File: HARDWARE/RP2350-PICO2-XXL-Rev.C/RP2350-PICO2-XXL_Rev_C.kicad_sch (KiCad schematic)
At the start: 83 parts, among them Q1 Q12MHz/18pF/30ppm/4P/3.2x2.5m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, U1 W25Q128JVSIQ(SOIC-8_208mils), U2 TPS62A02ADRLR(SOT-563-6), U3 RP2350B(QFN-80_10.00x10.00x0.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, U4 NA(W25Q128JVSIQ(SOIC-8_208mil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, U5 APS6404L-3SQR-SN(SOIC-8_150mi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

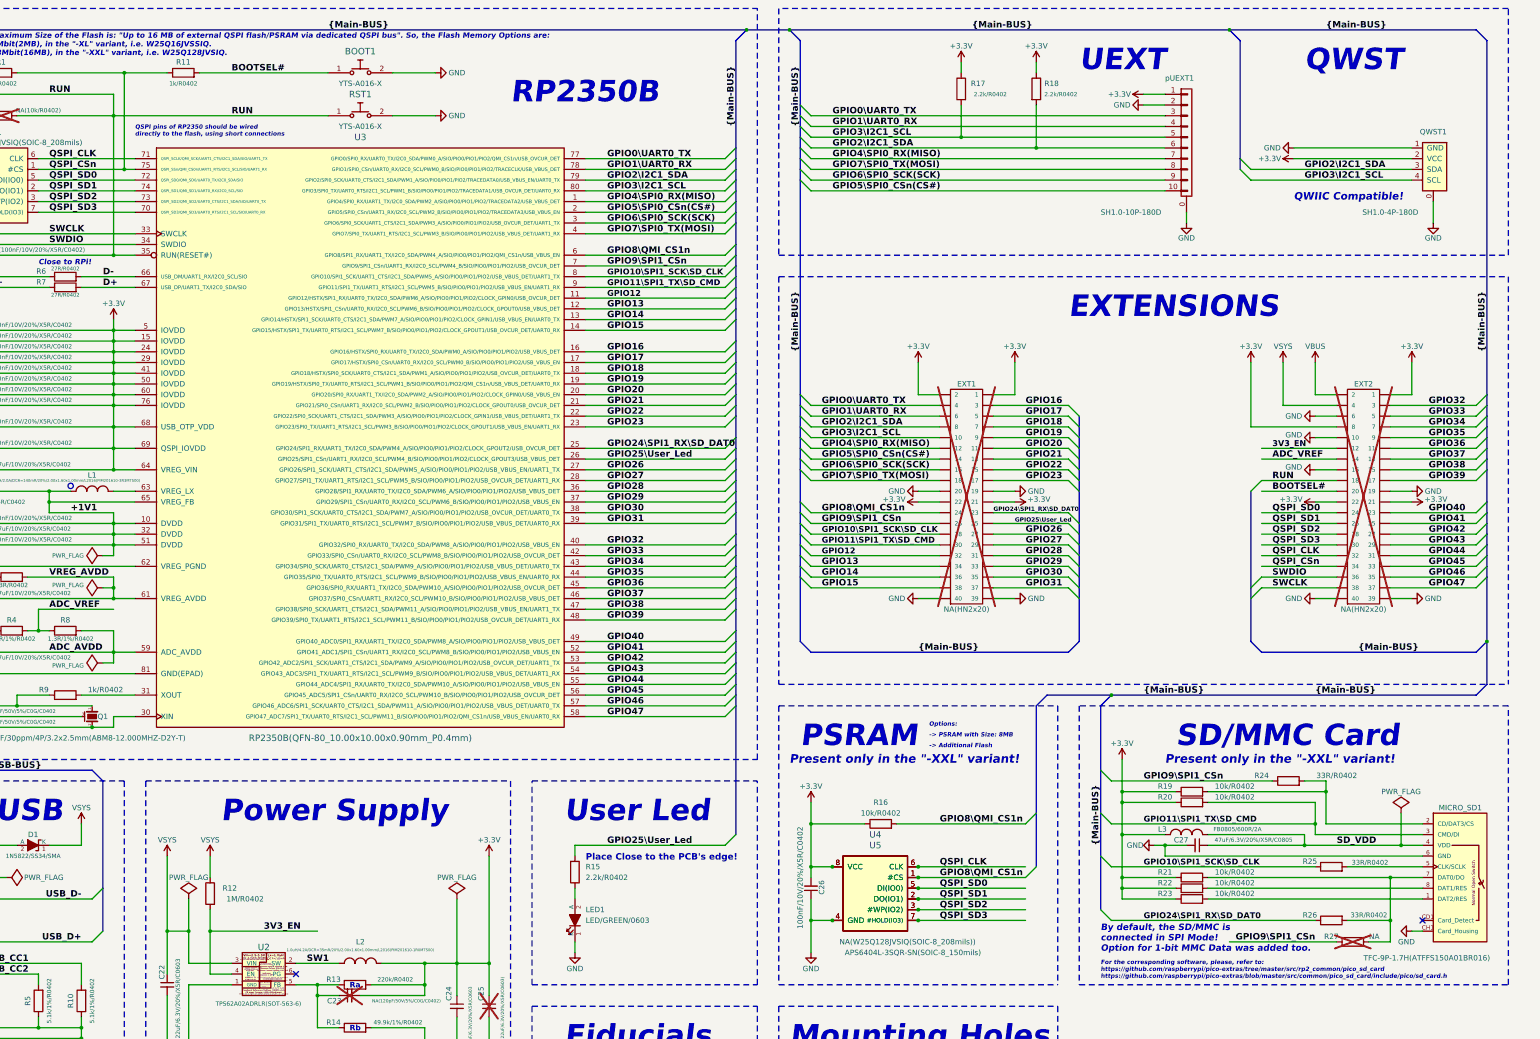
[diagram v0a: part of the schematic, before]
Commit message: removing unneeded connectors
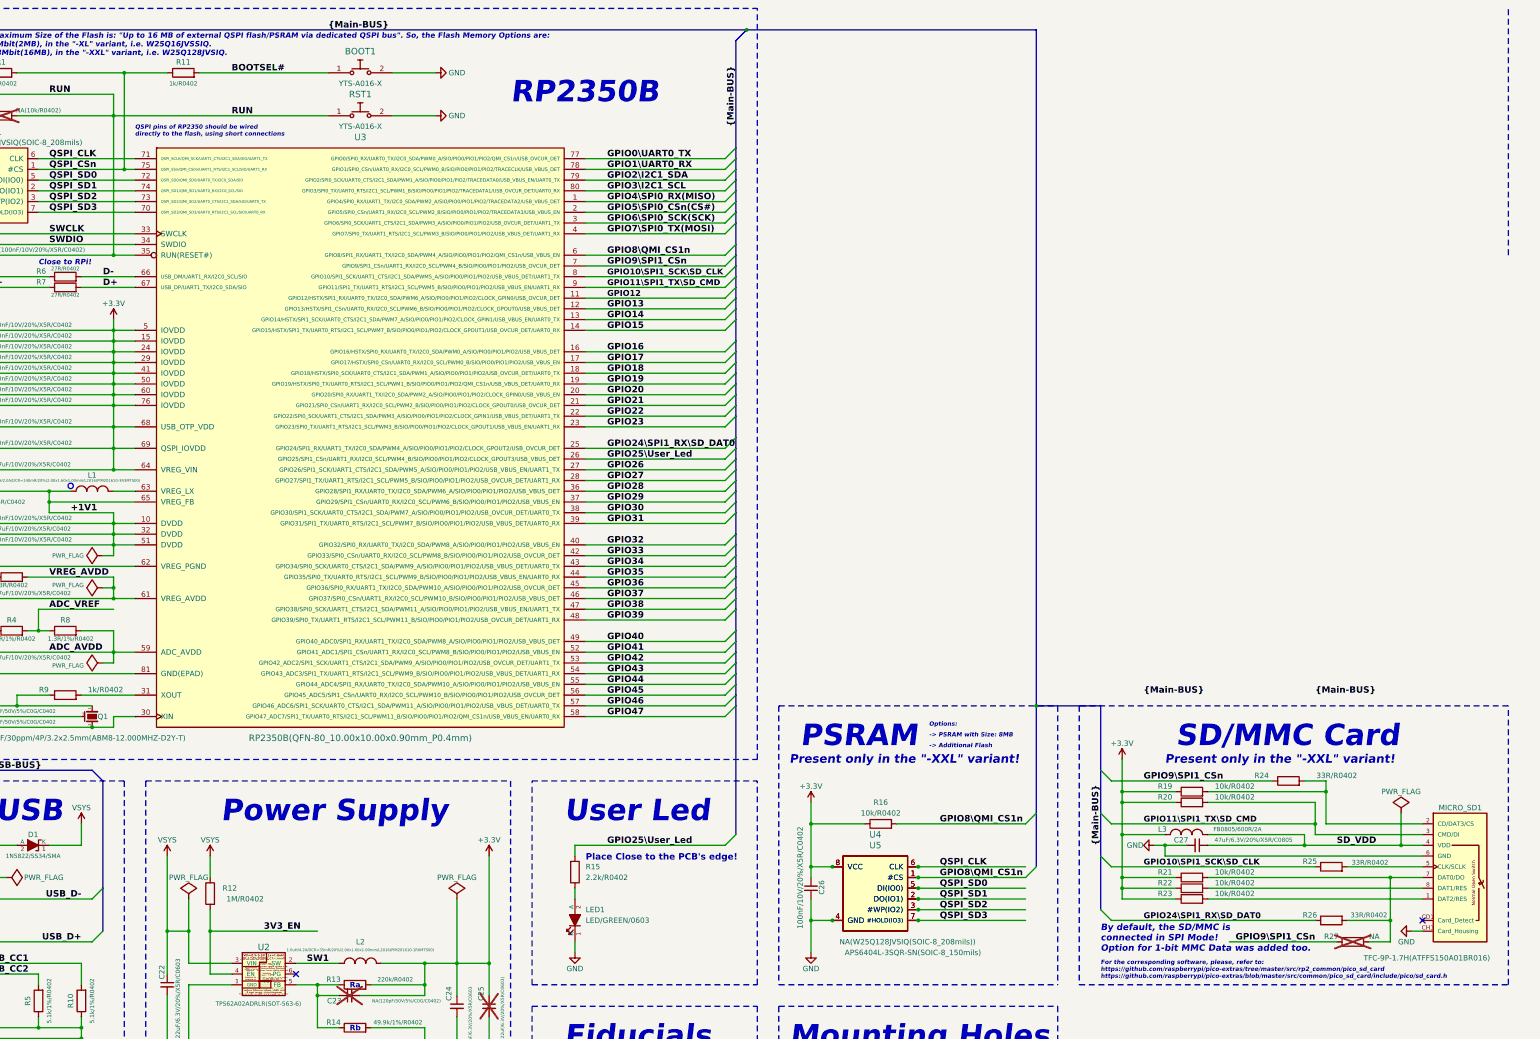
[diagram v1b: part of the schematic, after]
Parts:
- removed EXT1, EXT2: NA(HN2x20), OLIMEX_Connectors-FP:HN2x20, symbol OLIMEX_Connectors:BH40S
- removed QWST1: SH1.0-4P-180D, OLIMEX_Connectors-FP:BM04B-SRSS-TB, symbol OLIMEX_Connectors:QWST
- removed R17, R18: 2.2k/R0402, OLIMEX_RLC-FP:R_0402_5MIL_DWS, symbol OLIMEX_RCL:R
- removed pUEXT1: SH1.0-10P-180D, OLIMEX_Connectors-FP:BM10B-SRSS-TB, symbol OLIMEX_Connectors:CONN_01X10
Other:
- note removed: "EXTENSIONS"
- note removed: "QWIIC Compatible!"
- note removed: "QWST"
- note removed: "UEXT"

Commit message: routed psram and flash
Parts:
- removed C22, C24: 22uF/6.3V/20%/X5R/C0603, OLIMEX_RLC-FP:C_0603_5MIL_DWS, symbol OLIMEX_RCL:C
- removed C23: NA(120pF/50V/5%/C0G/C0402), OLIMEX_RLC-FP:C_0402_5MIL_DWS, symbol OLIMEX_RCL:C
- removed C25: NA(22uF/6.3V/20%/X5R/C0603), OLIMEX_RLC-FP:C_0603_5MIL_DWS, symbol OLIMEX_RCL:C
- removed FID1, FID4: Fiducial, OLIMEX_Other-FP:Fiducial1x3_Paste, symbol OLIMEX_OTHER:Fiducial
- removed FID2, FID3, FID5, FID6: Fiducial, OLIMEX_Other-FP:Fiducial1x3, symbol OLIMEX_OTHER:Fiducial
- removed L2: 1.0uH/4.2A/DCR=35mR/20%/2.00x1.60x1.00mm/L2016(PI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, OLIMEX_RLC-FP:L_2016_MM, symbol OLIMEX_RCL:L
- removed R12: 1M/R0402, OLIMEX_RLC-FP:R_0402_5MIL_DWS, symbol OLIMEX_RCL:R
- removed R13: 220k/R0402, OLIMEX_RLC-FP:R_0402_5MIL_DWS, symbol OLIMEX_RCL:R
- removed R14: 49.9k/1%/R0402, OLIMEX_RLC-FP:R_0402_5MIL_DWS, symbol OLIMEX_RCL:R
- removed U2: TPS62A02ADRLR(SOT-563-6), OLIMEX_Regulators-FP:SOT-563-6, symbol OLIMEX_Regulators:TPS62A02ADRLR(SOT-563-6)
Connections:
- no-connect marks 4 -> 3
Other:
- note removed: "Fiducials"
- note removed: "Ra"
- note removed: "Rb"
- note removed: "Vout=0.6*(1+Ra/Rb)"

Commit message: WIP: osc placed, need to add global osc with match length timing
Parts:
- removed C21: 27pF/50V/5%/C0G/C0402, OLIMEX_RLC-FP:C_0402_5MIL_DWS, symbol OLIMEX_RCL:C
- removed C27: 47uF/6.3V/20%/X5R/C0805, OLIMEX_RLC-FP:C_0805_5MIL_DWS, symbol OLIMEX_RCL:C
- removed L3: FB0805/600R/2A, OLIMEX_RLC-FP:L_0805_5MIL_DWS, symbol OLIMEX_RCL:L
- removed MICRO_SD1: TFC-9P-1.7H(ATFFS150A01BR016), OLIMEX_Connectors-FP:uSD(TFC-9P-1.xH(ATFFS150A01BR016)), symbol OLIMEX_Connectors:MICRO_SD(TFC-9P-1.xH(ATFFS150A01BR016))
- removed Q1: Q12MHz/18pF/30ppm/4P/3.2x2.5mm(ABM8-12.000MHZ-D2Y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, OLIMEX_Crystal-FP:TSX-3.2x2.5mm_GND(3), symbol OLIMEX_Devices:Crystal_GND
- removed R19, R20, R21, R22, R23: 10k/R0402, OLIMEX_RLC-FP:R_0402_5MIL_DWS, symbol OLIMEX_RCL:R
- removed R24, R25, R26: 33R/R0402, OLIMEX_RLC-FP:R_0402_5MIL_DWS, symbol OLIMEX_RCL:R
- removed R27: NA, OLIMEX_RLC-FP:R_0402_5MIL_DWS, symbol OLIMEX_RCL:R
- removed R9: 1k/R0402, OLIMEX_RLC-FP:R_0402_5MIL_DWS, symbol OLIMEX_RCL:R
- added JP1: (no value), PCM_SparkFun-Jumper:Jumper_3_NO_NoSilk, symbol PCM_SparkFun-Jumper:SolderJumper_3_Open_No_Silk
- added X1: SMD2520-4, PCM_Crystal_AKL:Crystal_SMD_2520-4Pin_2.5x2.0mm, symbol PCM_Crystal_AKL:SMD2520-4
- C20: value 27pF/50V/5%/C0G/C0402 -> 100nF/10V/20%/X5R/C0402; footprint OLIMEX_RLC-FP:C_0402_5MIL_DWS -> KiCad:C_0402_5MIL_DWS
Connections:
- net +3.3V: now also C20.2, JP1.3 (C), X1.4
- net GND: now also C20.1, JP1.1 (A), X1.2; no longer C20.2
- net at U3.30 (XIN): now also X1.3
- new net: JP1.2 (B), X1.1
- no-connect marks 3 -> 2
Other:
- note removed: "By default, the SD/MMC is connected in SPI Mode! Option for 1-bit MMC Data was added too."
- note removed: "For the corresponding software, please, refer to: https://github.com/raspberrypi/pico-extras/tree/master/src/rp2_common/pico_sd_card https://github.com/raspberrypi/pico-extras/blob/master/src/common/pico_sd_card/include/pico/sd_card.h"
- note removed: "SD/MMC Card"
